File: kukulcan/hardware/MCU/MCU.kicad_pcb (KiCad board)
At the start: 4 copper layers, 90 x 110 mm, 86 parts, among them J1 Barrel_Jack_5V_In, J2 Barrel_Jack_5V_In, J3 MiniPCIe Socket, J4 USB_C_Receptacle, J5 SMA_GNSS, Q1 AO3401A, U1 NEO-M8N, U2 ESP32-S3R16V, U3 W25Q256JWEIQ, U4 TLV1117-33, U5 BMI088, U6 BME280, U8 BNO055, X1 40MHz, Y1 32.768kHz

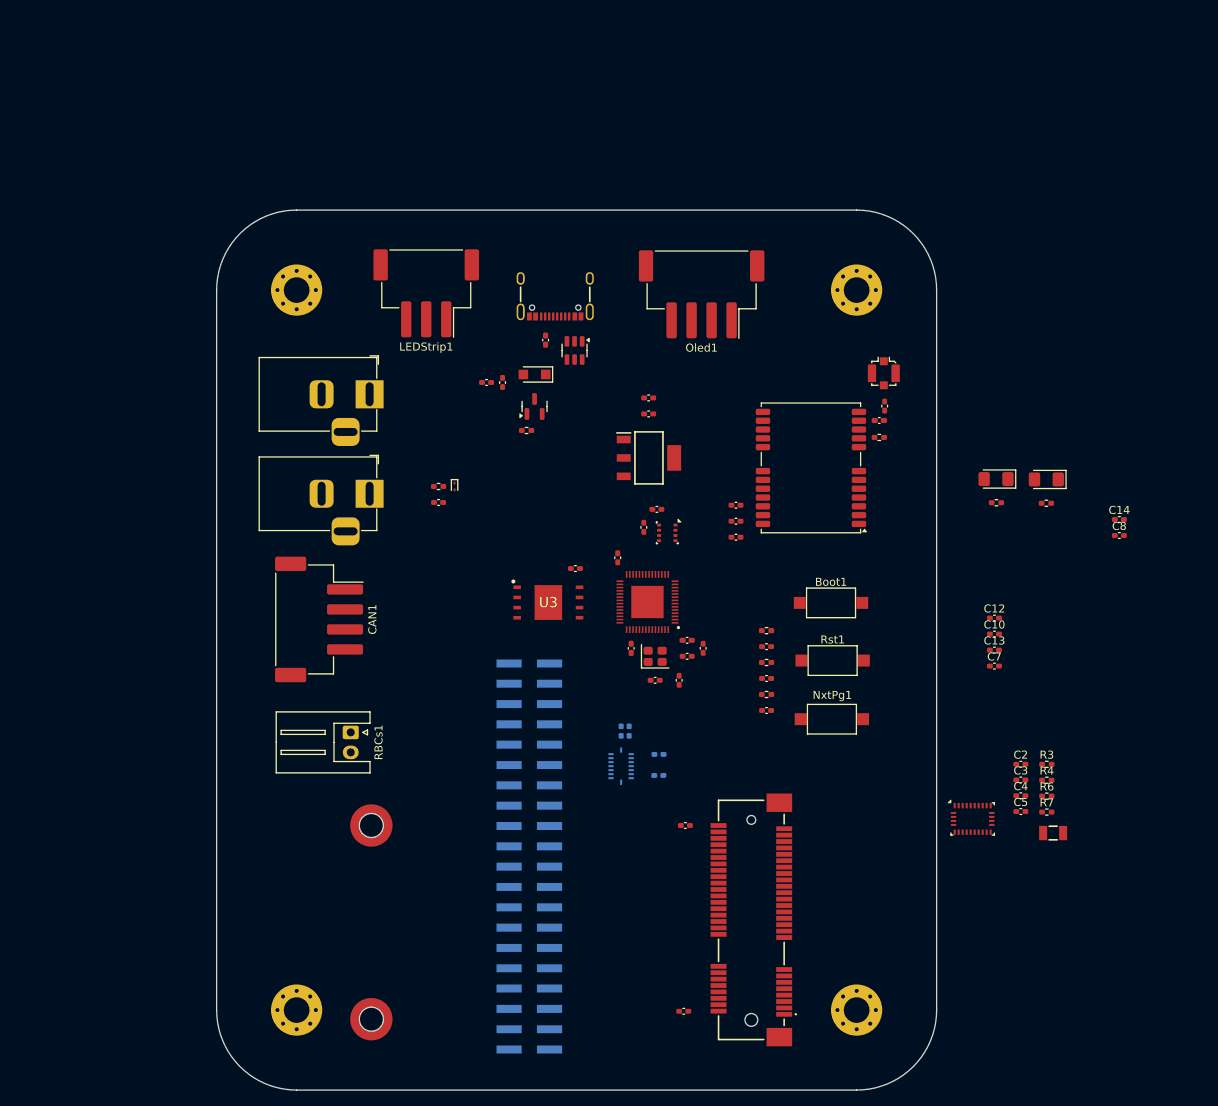
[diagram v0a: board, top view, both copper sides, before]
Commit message: feat(kukulcan): several layout and schematic improvements, tasks pending. PCIe connector out.
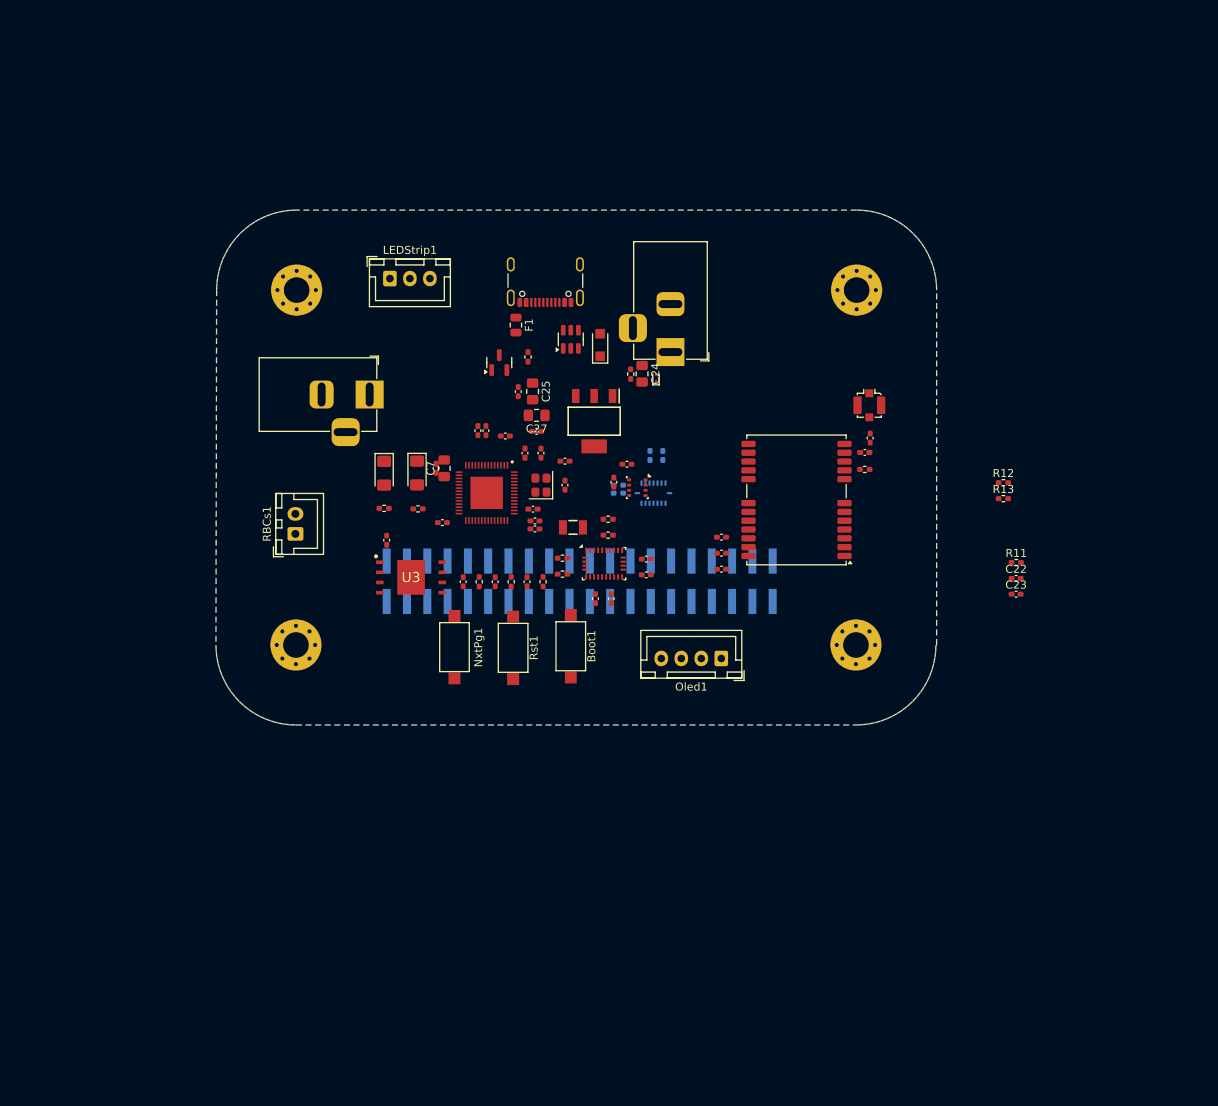
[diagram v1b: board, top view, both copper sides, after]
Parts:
- removed CAN1: JST XH 01x04, Connector_JST:JST_XH_S4B-XH-SM4-TB_1x04-1MP_P2.50mm_Horizontal
- removed J3: MiniPCIe Socket, Core_System_2026:MiniPCIeSocket
- removed REF** (x2): STAND-OFF-REFLOW-M2.0, PCM_SparkFun-Hardware:Standoff_Reflow-M2.0
- added R11: 0R, Resistor_SMD:R_0402_1005Metric_Pad0.72x0.64mm_HandSolder, F.Cu at (188.2, 98.5)
- added R12: 5k1, Resistor_SMD:R_0402_1005Metric_Pad0.72x0.64mm_HandSolder, F.Cu at (186.6, 88.5)
- added R13: 5k1, Resistor_SMD:R_0402_1005Metric_Pad0.72x0.64mm_HandSolder, F.Cu at (186.6, 90.5)
- C22: value 10uF -> 470nF
- C23: value 0.1uF -> 470nF
- C24, C25, C27, C7: footprint Capacitor_SMD:C_0402_1005Metric_Pad0.74x0.62mm_HandSolder -> Capacitor_SMD:C_0805_2012Metric_Pad1.18x1.45mm_HandSolder
- F1: footprint Fuse:Fuse_0402_1005Metric_Pad0.77x0.64mm_HandSolder -> Fuse:Fuse_0805_2012Metric
- J4: footprint PCM_SparkFun-Connector:USB-C_16 -> Connector_USB:USB_C_Receptacle_GCT_USB4105-xx-A_16P_TopMnt_Horizontal
- LEDStrip1: footprint Connector_JST:JST_XH_S3B-XH-SM4-TB_1x03-1MP_P2.50mm_Horizontal -> Connector_JST:JST_XH_B3B-XH-A_1x03_P2.50mm_Vertical
- Oled1: footprint Connector_JST:JST_XH_S4B-XH-SM4-TB_1x04-1MP_P2.50mm_Horizontal -> Connector_JST:JST_XH_B4B-XH-A_1x04_P2.50mm_Vertical
- RBCs1: footprint Connector_JST:JST_XH_S2B-XH-A_1x02_P2.50mm_Horizontal -> Connector_JST:JST_XH_B2B-XH-A_1x02_P2.50mm_Vertical
- moved LED1 78.7 mm to (113.3, 87.3), turned to -90 degrees
- moved R23 78.6 mm to (113.4, 91.8)
- moved R2 76.5 mm to (109.2, 91.7)
- moved LED2 76.5 mm to (109.2, 87.3), turned to -90 degrees
- moved C13 73.4 mm to (115.7, 86.7), turned to 90 degrees
- moved C7 73.1 mm to (116.7, 86.7), turned to 90 degrees
- moved C8 73.1 mm to (128.0, 94.3)
- moved C14 73.1 mm to (128.0, 93.3)
- moved Y1 71.2 mm to (132.8, 94.1)
- moved C12 68.7 mm to (120.9, 82.0), turned to 90 degrees
- moved C10 68.5 mm to (121.9, 82.0), turned to 90 degrees
- moved C23 66.7 mm to (188.2, 102.5)
- moved R3 65.8 mm to (131.5, 98.0)
- moved R4 65.8 mm to (131.5, 100.0)
- moved R6 64.8 mm to (137.2, 93.1)
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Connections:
- net Net-(C6-Pad2) renamed /XTAL_P
- net Net-(U2-XTAL_N) renamed /XTAL_N
- net Net-(U8-XIN32) renamed /XIN32
- net Net-(U8-XOUT32) renamed /XOUT32
- C22 pad 1: +3V3 -> GND
- C22 pad 2: GND -> +VUSB
- C23 pad 1: +3V3 -> GND
- C23 pad 2: GND -> +VUSBF
- D1 pad 1: Net-(U2-GPIO19/USB_D-) -> /USBCD-
- D1 pad 3: Net-(U2-GPIO20/USB_D+) -> /USBCD+
- D1 pad 4: Net-(D1-I/O2-Pad4) -> /USBD+
- D1 pad 6: Net-(D1-I/O1-Pad6) -> /USBD-
- J4 pad A5: unconnected-(J4-CC1-PadA5) -> /USBCC1
- J4 pad A6: Net-(D1-I/O2-Pad4) -> /USBCD+
- J4 pad A7: Net-(D1-I/O1-Pad6) -> /USBCD-
- J4 pad B5: unconnected-(J4-CC2-PadB5) -> /USBCC2
- J4 pad B6: Net-(D1-I/O2-Pad4) -> /USBCD+
- J4 pad B7: Net-(D1-I/O1-Pad6) -> /USBCD-
- Jetson1 pad 10: unconnected-(Jetson1-Pin_10-Pad10) -> JT_RX
- Jetson1 pad 14: unconnected-(Jetson1-Pin_14-Pad14) -> GND
- Jetson1 pad 20: unconnected-(Jetson1-Pin_20-Pad20) -> GND
- Jetson1 pad 25: unconnected-(Jetson1-Pin_25-Pad25) -> GND
- Jetson1 pad 27: unconnected-(Jetson1-Pin_27-Pad27) -> SDA
- Jetson1 pad 28: unconnected-(Jetson1-Pin_28-Pad28) -> SCL
- Jetson1 pad 29: unconnected-(Jetson1-Pin_29-Pad29) -> GPIO01_JT
- Jetson1 pad 3: unconnected-(Jetson1-Pin_3-Pad3) -> SDA
- Jetson1 pad 30: unconnected-(Jetson1-Pin_30-Pad30) -> GND
- Jetson1 pad 31: unconnected-(Jetson1-Pin_31-Pad31) -> GPIO10_JT
- Jetson1 pad 34: unconnected-(Jetson1-Pin_34-Pad34) -> GND
- Jetson1 pad 39: unconnected-(Jetson1-Pin_39-Pad39) -> GND
- Jetson1 pad 5: unconnected-(Jetson1-Pin_5-Pad5) -> SCL
- Jetson1 pad 6: unconnected-(Jetson1-Pin_6-Pad6) -> GND
- Jetson1 pad 7: unconnected-(Jetson1-Pin_7-Pad7) -> GPIO09_JT
- Jetson1 pad 8: unconnected-(Jetson1-Pin_8-Pad8) -> JT_TX
- Jetson1 pad 9: unconnected-(Jetson1-Pin_9-Pad9) -> GND
- RBCs1 pad 1: RX -> RB_RX
- RBCs1 pad 2: TX -> RB_TX
- U2 pad 25: Net-(U2-GPIO19/USB_D-) -> /USBD-
- U2 pad 26: Net-(U2-GPIO20/USB_D+) -> /USBD+
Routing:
- added copper zone on In2.Cu, net +3V3
- added copper zone on In2.Cu, net +RB_VDD_5V
- added copper zone on In2.Cu, net +VDD_5V
- added copper zone on In1.Cu, net GND
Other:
- board size 90 x 110 mm -> 90.1 x 64.4 mm
- rule pad_to_mask_clearance: 0.05 -> 0.1

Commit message: feat(kukulcan): current beta
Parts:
- removed the C22 at (188.2, 100.5)
- removed the C23 at (188.2, 102.5)
- removed the R11 at (188.2, 98.5)
- removed the R12 at (186.6, 88.5)
- removed the R13 at (186.6, 90.5)
- added C28: 0.1uF, Capacitor_SMD:C_0402_1005Metric_Pad0.74x0.62mm_HandSolder, F.Cu at (187.8, 94.8)
- added C29: 0.1uF, Capacitor_SMD:C_0402_1005Metric_Pad0.74x0.62mm_HandSolder, F.Cu at (187.8, 96.8)
- added R5: 5k1, Resistor_SMD:R_0402_1005Metric_Pad0.72x0.64mm_HandSolder, F.Cu at (184.5, 94.9)
- added R6: 5k1, Resistor_SMD:R_0402_1005Metric_Pad0.72x0.64mm_HandSolder, F.Cu at (184.5, 96.8)
- turned U3 to 180 degrees
- renumbered C15 to C1, C14 to C10, C24 to C11, C25 to C12, C26 to C13, C27 to C14, C28 to C15, C6 to C16, C11 to C17, C13 to C2, C1 to C20, C2 to C21, C3 to C22, C4 to C23, C38 to C24, C37 to C25, C36 to C26, C5 to C27, C9 to C3, C35 to C30, C34 to C31, C39 to C32, C7 to C4, C16 to C5, C17 to C6, C8 to C7, C10 to C8, C12 to C9, D2 to D1, D5 to D2, D1 to D3, J2 to J1, J1 to J2, J4 to J3, J5 to J4, L2 to L1, L4 to L2, L1 to L3, R16 to R1, R6 to R10, R3 to R11, R4 to R12, R7 to R13, R26 to R14, R9 to R15, R10 to R16, R17 to R2, R23 to R3, R2 to R4, R5 to R7, R1 to R9, U4 to U1, U3 to U2, U2 to U3, U8 to U4, U1 to U5, U5 to U6, U6 to U7
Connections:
- net GPIO09_JT renamed JTMCU1
- net GPIO10_JT renamed GPIO11_JT
- C16 pad 2: /XTAL_P -> Net-(C16-Pad2)
- L2 pad 1: /XTAL_P -> Net-(C16-Pad2)
- L2 pad 2: Net-(U2-XTAL_P) -> /XTAL_P
- U3 pad 54: Net-(U2-XTAL_P) -> /XTAL_P
- X1 pad 1: /XTAL_P -> Net-(C16-Pad2)

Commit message: feat(kukulcan): final schematic draft
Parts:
- removed the C20 at (144.0, 85.1)
- removed the C21 at (142.4, 85.1)
- added FID1: Fiducial, Fiducial:Fiducial_Cross_1.5mm_Mask2mm, F.Cu at (187.3, 108.7)
- added FID2: Fiducial, Fiducial:Fiducial_Cross_1.5mm_Mask2mm, F.Cu at (187.3, 112.3)
- added FID3: Fiducial, Fiducial:Fiducial_Cross_1.5mm_Mask2mm, F.Cu at (190.8, 108.7)
- added FID4: Fiducial, Fiducial:Fiducial_Cross_1.5mm_Mask2mm, F.Cu at (190.8, 112.3)
- added FID5: Fiducial, Fiducial:Fiducial_Cross_1.5mm_Mask2mm, F.Cu at (194.4, 108.7)
- added FID6: Fiducial, Fiducial:Fiducial_Cross_1.5mm_Mask2mm, F.Cu at (194.4, 112.3)
- added R11: 5k1, Resistor_SMD:R_0805_2012Metric_Pad1.20x1.40mm_HandSolder, F.Cu at (191.9, 78.6)
- added R12: 5k1, Resistor_SMD:R_0805_2012Metric_Pad1.20x1.40mm_HandSolder, F.Cu at (194.9, 79.6)
- C1, C10, C13, C15, C16, C17, C18, C19, C2, C20, C21, C22, C23, C24, C25, C26, C27, C3, C30, C31, C32, C5, C6, C7, C8, C9: footprint Capacitor_SMD:C_0402_1005Metric_Pad0.74x0.62mm_HandSolder -> Capacitor_SMD:C_0805_2012Metric_Pad1.18x1.45mm_HandSolder
- C28, C29: footprint Capacitor_SMD:C_0402_1005Metric_Pad0.74x0.62mm_HandSolder -> Capacitor_SMD:C_0805_2012Metric_Pad1.18x1.45mm_HandSolder; moved to B.Cu
- H1, H2, H3, H4: value MountingHole -> MountingHole_Pad; footprint MountingHole:MountingHole_3.2mm_M3_Pad_Via -> MountingHole:MountingHole_3.2mm_M3_Pad_TopBottom
- L1, L2, L3: footprint Inductor_SMD:L_0402_1005Metric_Pad0.77x0.64mm_HandSolder -> Inductor_SMD:L_0805_2012Metric_Pad1.05x1.20mm_HandSolder
- LED1, LED2: footprint LED_SMD:LED_1206_3216Metric_Pad1.42x1.75mm_HandSolder -> LED_SMD:LED_0805_2012Metric_Pad1.15x1.40mm_HandSolder
- R1, R10, R2, R3, R4, R5, R6, R7, R8, R9: footprint Resistor_SMD:R_0402_1005Metric_Pad0.72x0.64mm_HandSolder -> Resistor_SMD:R_0805_2012Metric_Pad1.20x1.40mm_HandSolder
- R13: renamed from R11; footprint Resistor_SMD:R_0402_1005Metric_Pad0.72x0.64mm_HandSolder -> Resistor_SMD:R_0805_2012Metric_Pad1.20x1.40mm_HandSolder
- R14: renamed from R12; footprint Resistor_SMD:R_0402_1005Metric_Pad0.72x0.64mm_HandSolder -> Resistor_SMD:R_0805_2012Metric_Pad1.20x1.40mm_HandSolder
- R15: renamed from R13; footprint Resistor_SMD:R_0402_1005Metric_Pad0.72x0.64mm_HandSolder -> Resistor_SMD:R_0805_2012Metric_Pad1.20x1.40mm_HandSolder
- R16: renamed from R14; footprint Resistor_SMD:R_0402_1005Metric_Pad0.72x0.64mm_HandSolder -> Resistor_SMD:R_0805_2012Metric_Pad1.20x1.40mm_HandSolder
- R17: renamed from R15; footprint Resistor_SMD:R_0402_1005Metric_Pad0.72x0.64mm_HandSolder -> Resistor_SMD:R_0805_2012Metric_Pad1.20x1.40mm_HandSolder
- R18: renamed from R16; footprint Resistor_SMD:R_0402_1005Metric_Pad0.72x0.64mm_HandSolder -> Resistor_SMD:R_0805_2012Metric_Pad1.20x1.40mm_HandSolder
- moved C2 94.3 mm to (209.7, 79.6), turned to 0 degrees
- moved C1 85.6 mm to (209.7, 76.6)
- moved L1 83.7 mm to (209.8, 95.6), turned to 0 degrees
- moved L2 82.2 mm to (209.8, 98.3), turned to 0 degrees
- moved C4 81.4 mm to (195.3, 65.6), turned to 0 degrees
- moved C16 78.2 mm to (209.7, 82.6), turned to 0 degrees
- moved C17 77.9 mm to (209.7, 85.6)
- moved C9 73.2 mm to (193.1, 70.2), turned to 180 degrees
- moved R6 70.8 mm to (121.6, 64.4), turned to 180 degrees
- moved H4 70.0 mm to (98.2, 108.8)
- moved H1 70.0 mm to (168.3, 64.5)
- moved R5 68.8 mm to (121.6, 67.0), turned to 180 degrees
- moved C14 68.2 mm to (195.4, 68.0), turned to 0 degrees
- moved C15 64.8 mm to (190.9, 65.5), turned to 0 degrees
- moved C3 64.4 mm to (191.0, 68.0), turned to 0 degrees
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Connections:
- H1 pad 1: (no net) -> GND
- H2 pad 1: (no net) -> GND
- H3 pad 1: (no net) -> GND
- H4 pad 1: (no net) -> GND
- Jetson1 pad 29: GPIO01_JT -> JT_MCU2
- Jetson1 pad 31: GPIO11_JT -> JT_MCU3
- Jetson1 pad 7: JTMCU1 -> JT_MCU1
- U1 pad 4: (no net) -> +3V3
- U3 pad 10: GPIO5 -> unconnected-(U3-GPIO5-Pad10)
- U3 pad 11: GPIO6 -> unconnected-(U3-GPIO6-Pad11)
- U3 pad 12: GPIO7 -> unconnected-(U3-GPIO7-Pad12)
- U3 pad 13: GPIO8 -> unconnected-(U3-GPIO8-Pad13)
- U3 pad 14: GPIO9 -> unconnected-(U3-GPIO9-Pad14)
- U3 pad 15: GPIO10 -> unconnected-(U3-GPIO10-Pad15)
- U3 pad 16: GPIO11 -> unconnected-(U3-GPIO11-Pad16)
- U3 pad 17: GPIO12 -> unconnected-(U3-GPIO12-Pad17)
- U3 pad 18: GPIO13 -> SDA
- U3 pad 19: GPIO14 -> SCL
- U3 pad 23: GPIO17 -> unconnected-(U3-GPIO17-Pad23)
- U3 pad 24: GPIO18 -> unconnected-(U3-GPIO18-Pad24)
- U3 pad 27: GPIO21 -> unconnected-(U3-GPIO21-Pad27)
- U3 pad 28: GPIO26 -> unconnected-(U3-SPICS1-Pad28)
- U3 pad 36: GPIO48 -> unconnected-(U3-SPICLK_N-Pad36)
- U3 pad 37: GPIO47 -> unconnected-(U3-SPICLK_P-Pad37)
- U3 pad 38: GPIO33 -> JT_MCU1
- U3 pad 39: GPIO34 -> JT_MCU2
- U3 pad 40: GPIO35 -> JT_MCU3
- U3 pad 41: GPIO36 -> LED_RED
- U3 pad 42: GPIO37 -> LED_WHITE
- U3 pad 43: GPIO38 -> LedStripGPIO
- U3 pad 44: GPIO39 -> unconnected-(U3-MTCK-Pad44)
- U3 pad 45: GPIO40 -> unconnected-(U3-MTDO-Pad45)
- U3 pad 47: GPIO41 -> RB_TX
- U3 pad 48: GPIO42 -> RB_RX
- U3 pad 51: GPIO45 -> unconnected-(U3-GPIO45-Pad51)
- U3 pad 52: GPIO46 -> unconnected-(U3-GPIO46-Pad52)
- U3 pad 6: GPIO1 -> NxtPg
- U3 pad 7: GPIO2 -> unconnected-(U3-GPIO2-Pad7)
- U3 pad 8: GPIO3 -> JT_TX
- U3 pad 9: GPIO4 -> JT_RX
- U4 pad 10: unconnected-(U4-BL_IND-Pad10) -> GND

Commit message: feat(kukulcan): partial final PCB draft, GNSS pending
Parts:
- removed R17, R18: 10k/5%, Resistor_SMD:R_0805_2012Metric_Pad1.20x1.40mm_HandSolder
- C1, C10, C11, C12, C13, C14, C15, C16, C17, C18, C19, C2, C20, C21, C22, C23, C24, C25, C26, C27, C28, C29, C3, C30, C31, C32, C4, C5, C6, C7, C8, C9: footprint Capacitor_SMD:C_0805_2012Metric_Pad1.18x1.45mm_HandSolder -> Capacitor_SMD:C_0603_1608Metric_Pad1.08x0.95mm_HandSolder
- FID4, FID5, FID6: moved to B.Cu
- H1, H2, H3, H4: footprint MountingHole:MountingHole_3.2mm_M3_Pad_TopBottom -> MountingHole:MountingHole_3.2mm_M3_Pad_Via
- L1, L2, L3: footprint Inductor_SMD:L_0805_2012Metric_Pad1.05x1.20mm_HandSolder -> Inductor_SMD:L_0603_1608Metric_Pad1.05x0.95mm_HandSolder
- R1, R10, R13, R15, R2, R3, R4, R5, R6, R7, R8, R9: footprint Resistor_SMD:R_0805_2012Metric_Pad1.20x1.40mm_HandSolder -> Resistor_SMD:R_0603_1608Metric_Pad0.98x0.95mm_HandSolder
- R11, R12: value 5k1 -> 10k/5%; footprint Resistor_SMD:R_0805_2012Metric_Pad1.20x1.40mm_HandSolder -> Resistor_SMD:R_0603_1608Metric_Pad0.98x0.95mm_HandSolder
- R14: value 10k/5% -> 10R/1%; footprint Resistor_SMD:R_0805_2012Metric_Pad1.20x1.40mm_HandSolder -> Resistor_SMD:R_0603_1608Metric_Pad0.98x0.95mm_HandSolder
- R16: value 10R/1% -> 10k/5%; footprint Resistor_SMD:R_0805_2012Metric_Pad1.20x1.40mm_HandSolder -> Resistor_SMD:R_0603_1608Metric_Pad0.98x0.95mm_HandSolder
- moved C12 94.8 mm to (169.1, 117.5), turned to 180 degrees
- moved D2 93.8 mm to (173.2, 118.0), turned to 0 degrees
- moved C13 92.2 mm to (169.1, 116.0), turned to 180 degrees
- moved R4 84.7 mm to (135.1, 126.8)
- moved R3 83.0 mm to (131.1, 126.8)
- moved LED2 79.8 mm to (135.8, 124.0), turned to 90 degrees
- moved LED1 78.3 mm to (131.7, 124.0), turned to 90 degrees
- moved J1 72.3 mm to (177.0, 97.0), turned to 180 degrees
- moved FID4 71.8 mm to (125.8, 82.0), turned to 180 degrees
- moved RBCs1 70.5 mm to (161.5, 125.8), turned to 180 degrees
- moved R12 70.4 mm to (134.8, 116.2), turned to 0 degrees
- moved R11 69.2 mm to (134.8, 117.8), turned to 0 degrees
- moved D1 68.9 mm to (173.0, 107.5)
- moved J3 68.3 mm to (148.0, 128.0), turned to 0 degrees
- moved Q1 67.8 mm to (172.9, 114.9)
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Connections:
- J3 pad A1: (no net) -> GND
- J3 pad A12: (no net) -> GND
- J3 pad A4: (no net) -> +VUSB
- J3 pad A9: (no net) -> +VUSB
- J3 pad B1: (no net) -> GND
- J3 pad B12: (no net) -> GND
- J3 pad B4: (no net) -> +VUSB
- J3 pad B9: (no net) -> +VUSB
- Jetson1 pad 27: SDA -> unconnected-(Jetson1-Pin_27-Pad27)
- Jetson1 pad 28: SCL -> unconnected-(Jetson1-Pin_28-Pad28)
- Jetson1 pad 29: JT_MCU2 -> JT_MCU1
- Jetson1 pad 31: JT_MCU3 -> JT_MCU2
- Jetson1 pad 7: JT_MCU1 -> unconnected-(Jetson1-Pin_7-Pad7)
- LEDStrip1 pad 2: LedStripGPIO -> LedStrip
- R11 pad 1: +3V3 -> GND
- R11 pad 2: SDA -> Net-(U4-PS0)
- R12 pad 1: +3V3 -> GND
- R12 pad 2: SCL -> Net-(U4-PS1)
- R13 pad 2: Net-(U4-PS0) -> Net-(U4-COM3)
- R14 pad 1: GND -> Net-(U5-VCC_RF)
- R14 pad 2: Net-(U4-PS1) -> Net-(L3-Pad1)
- R15 pad 1: GND -> SCL
- R15 pad 2: Net-(U4-COM3) -> +3V3
- R16 pad 1: Net-(U5-VCC_RF) -> SDA
- R16 pad 2: Net-(L3-Pad1) -> +3V3
- U2 pad 9: (no net) -> GND
- U3 pad 11: unconnected-(U3-GPIO6-Pad11) -> JT_MCU1
- U3 pad 13: unconnected-(U3-GPIO8-Pad13) -> JT_TX
- U3 pad 14: unconnected-(U3-GPIO9-Pad14) -> JT_RX
- U3 pad 15: unconnected-(U3-GPIO10-Pad15) -> SDA
- U3 pad 16: unconnected-(U3-GPIO11-Pad16) -> SCL
- U3 pad 18: SDA -> unconnected-(U3-GPIO13-Pad18)
- U3 pad 19: SCL -> unconnected-(U3-GPIO14-Pad19)
- U3 pad 38: JT_MCU1 -> LED_WHITE
- U3 pad 39: JT_MCU2 -> LED_RED
- U3 pad 40: JT_MCU3 -> RB_TX
- U3 pad 41: LED_RED -> RB_RX
- U3 pad 42: LED_WHITE -> LedStrip
- U3 pad 43: LedStripGPIO -> unconnected-(U3-GPIO38-Pad43)
- U3 pad 47: RB_TX -> unconnected-(U3-MTDI-Pad47)
- U3 pad 48: RB_RX -> unconnected-(U3-MTMS-Pad48)
- U3 pad 8: JT_TX -> unconnected-(U3-GPIO3-Pad8)
- U3 pad 9: JT_RX -> JT_MCU2
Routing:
- net GND: track 0.00 -> 167.8 mm, vias 0 -> 124
- net SCL: track 0.00 -> 88.6 mm
- net SDA: track 0.00 -> 74.3 mm, vias 0 -> 2
- net +3V3: track 0.00 -> 61.9 mm, vias 0 -> 48
- net +VDD_5V: track 0.00 -> 41.2 mm, vias 0 -> 10
- net LedStrip: track 0.00 -> 40.1 mm
- net LED_WHITE: track 0.00 -> 40.0 mm, vias 0 -> 2
- net LED_RED: track 0.00 -> 34.8 mm, vias 0 -> 2
- net JT_TX: track 0.00 -> 31.4 mm, vias 0 -> 1
- net JT_RX: track 0.00 -> 27.5 mm, vias 0 -> 1
- net RB_RX: track 0.00 -> 20.1 mm
- net RB_TX: track 0.00 -> 20.1 mm
- net +RB_VDD_5V: track 0.00 -> 19.1 mm, vias 0 -> 7
- net RST: track 0.00 -> 18.4 mm
- net NxtPg: track 0.00 -> 16.4 mm
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- added copper zone on B.Cu, net +3V3
- added copper zone on F.Cu, net +3V3
- added copper zone on B.Cu, net +RB_VDD_5V
- added copper zone on F.Cu, net +RB_VDD_5V
- added copper zone on B.Cu, net +VDD_5V
- added copper zone on F.Cu, net +VDD_5V
- added copper zone on B.Cu, net GND
- added copper zone on F.Cu, net GND
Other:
- board size 90.1 x 64.4 mm -> 78 x 53 mm
